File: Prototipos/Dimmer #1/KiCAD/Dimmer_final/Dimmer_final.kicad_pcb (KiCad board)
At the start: 2 copper layers, 50 x 100 mm, 1 part

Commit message: Avances PCB dimmer
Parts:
- removed the REF** at (95.5, 78.5)
- added C1: 330nF, Capacitor_THT:C_Disc_D10.5mm_W5.0mm_P7.50mm, F.Cu at (103.2, 56.5)
- added C2: 10nF, Capacitor_THT:C_Disc_D10.5mm_W5.0mm_P7.50mm, F.Cu at (130.8, 71.0)
- added D1: DB3, Diode_THT:D_DO-35_SOD27_P7.62mm_Horizontal, F.Cu at (103.5, 66.5)
- added D2: D_Small, Diode_THT:D_DO-41_SOD81_P7.62mm_Horizontal, F.Cu at (117.8, 127.1)
- added D3: D_Small, Diode_THT:D_DO-41_SOD81_P7.62mm_Horizontal, F.Cu at (123.5, 75.2)
- added J2: Conn_01x02, TerminalBlock_Phoenix:TerminalBlock_Phoenix_MKDS-1,5-2-5.08_1x02_P5.08mm_Horizontal, F.Cu at (137.5, 107.6)
- added J4: ~, Proyecto_Final:BUS_PCIE_x4_NSH, F.Cu at (95.5, 78.5)
- added K1: SRD-05VDC-SL-C, Relay_THT:Relay_SPDT_SANYOU_SRD_Series_Form_C, F.Cu at (113.5, 73.5)
- added Q1: BC548B, Package_TO_SOT_THT:TO-92_Inline_Wide, F.Cu at (123.5, 85.5)
- added Q2: BT137, Package_TO_SOT_THT:TO-220-3_Horizontal_TabDown, F.Cu at (137.1, 75.0)
- added R1: 47k, Resistor_THT:R_Axial_DIN0207_L6.3mm_D2.5mm_P7.62mm_Horizontal, F.Cu at (103.7, 60.5)
- added R10: 10k, Resistor_THT:R_Axial_DIN0207_L6.3mm_D2.5mm_P7.62mm_Horizontal, F.Cu at (107.2, 134.0)
- added R11: 33k, Resistor_THT:R_Axial_DIN0207_L6.3mm_D2.5mm_P7.62mm_Horizontal, F.Cu at (107.2, 137.5)
- added R2: 12k, Resistor_THT:R_Axial_DIN0207_L6.3mm_D2.5mm_P7.62mm_Horizontal, F.Cu at (116.0, 94.0)
- added R3: 100k, Potentiometer_THT:Potentiometer_Alps_RK09K_Single_Vertical, F.Cu at (117.5, 67.0)
- added R4: 470, Resistor_THT:R_Axial_DIN0207_L6.3mm_D2.5mm_P7.62mm_Horizontal, F.Cu at (111.3, 63.5)
- added R5: 82, Resistor_THT:R_Axial_DIN0207_L6.3mm_D2.5mm_P7.62mm_Horizontal, F.Cu at (107.2, 109.2)
- added R6: 10k, Resistor_THT:R_Axial_DIN0207_L6.3mm_D2.5mm_P7.62mm_Horizontal, F.Cu at (107.2, 118.5)
- added R7: 82, Resistor_THT:R_Axial_DIN0207_L6.3mm_D2.5mm_P7.62mm_Horizontal, F.Cu at (107.2, 112.2)
- added R8: 10k, Resistor_THT:R_Axial_DIN0207_L6.3mm_D2.5mm_P7.62mm_Horizontal, F.Cu at (107.2, 128.0)
- added R9: 51, Resistor_THT:R_Axial_DIN0207_L6.3mm_D2.5mm_P7.62mm_Horizontal, F.Cu at (138.5, 66.5)
- added REF**: MountingHole_2mm, MountingHole:MountingHole_2mm, F.Cu at (96.0, 49.0)
- added REF**: MountingHole_2mm, MountingHole:MountingHole_2mm, F.Cu at (96.0, 141.0)
- added REF**: MountingHole_2mm, MountingHole:MountingHole_2mm, F.Cu at (138.0, 49.0)
- added REF**: MountingHole_2mm, MountingHole:MountingHole_2mm, F.Cu at (138.0, 141.0)
- added U1: MOC3021M, ProyectoFinal:DIP762W45P254L889H508Q6, F.Cu at (110.8, 103.0)
- added U2: EL817, Package_DIP:DIP-4_W7.62mm, F.Cu at (114.9, 124.5)
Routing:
- net AGND: track 0.00 -> 148.9 mm
- net 48Vca_L: track 0.00 -> 129.4 mm
- net 48Vca_N: track 0.00 -> 86.8 mm
- net LOAD_L: track 0.00 -> 71.2 mm
- net 3.3Vcc: track 0.00 -> 49.9 mm
- net Net-(D1-A): track 0.00 -> 45.0 mm
- net IDENT_V: track 0.00 -> 44.9 mm
- net RELAY_T2: track 0.00 -> 32.9 mm
- net 5Vcc: track 0.00 -> 31.5 mm, vias 0 -> 2
- net Net-(J4-HP_Power): track 0.00 -> 23.6 mm
- net UC_RELAY: track 0.00 -> 20.7 mm, vias 0 -> 2
- net Net-(Q2-G): track 0.00 -> 20.3 mm
- net Net-(K1-Pad3): track 0.00 -> 14.2 mm
- net unconnected-(J4-12Vdc-Pad4): track 0.00 -> 13.7 mm
- net Net-(R1-Pad2): track 0.00 -> 13.1 mm
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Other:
- board text added: "Control analógico"
- board text added: "Control digital"
- board text added: "Ident. módulo"
- board text added: "Relé con driver"
- board text added: "TRIAC y Snubber"
- board text added: "ZCD"

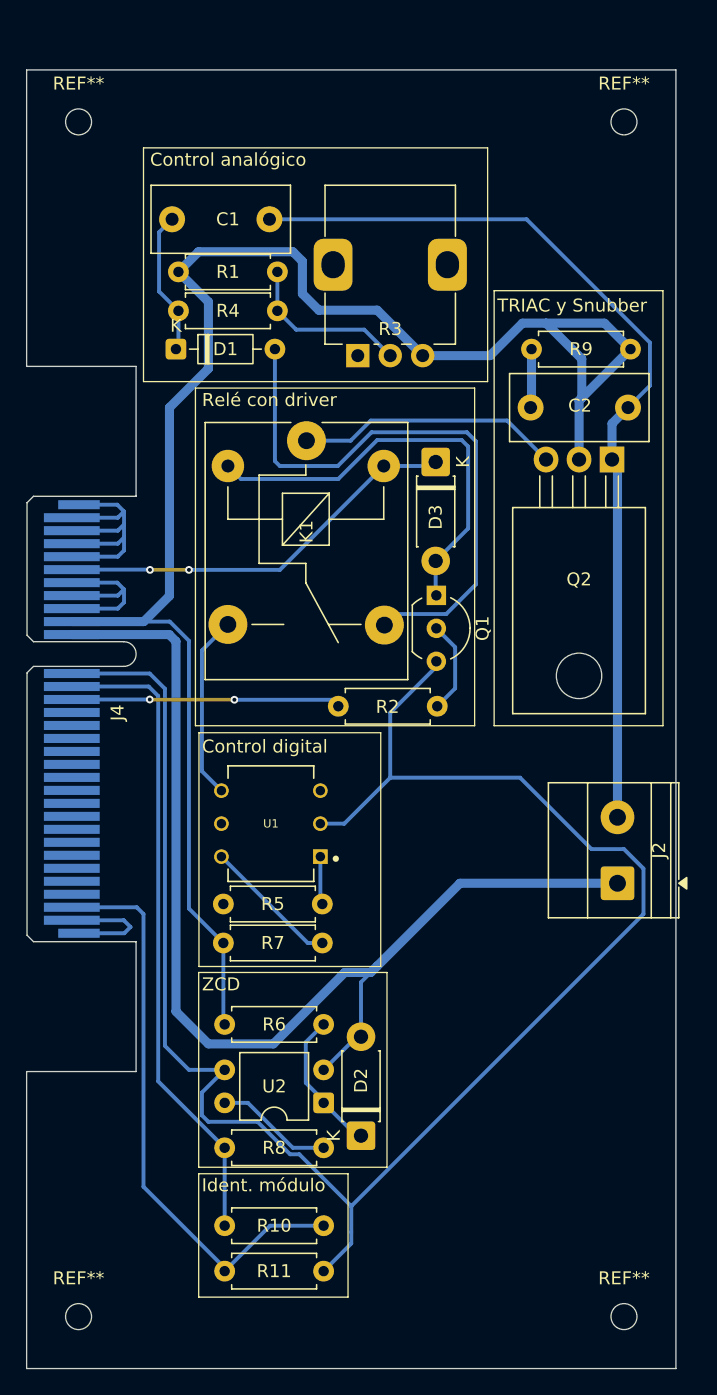
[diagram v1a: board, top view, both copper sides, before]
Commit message: Finalizar enrutamiento y primera versión inicial PCB
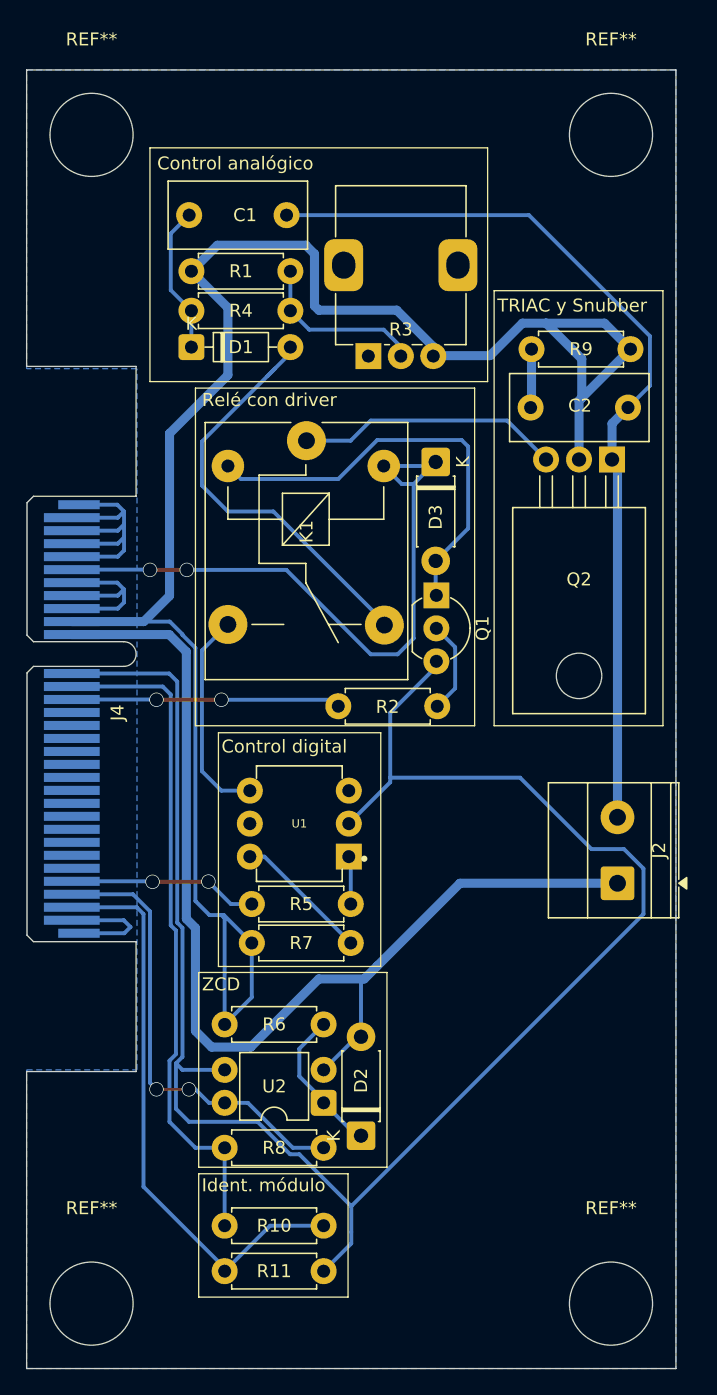
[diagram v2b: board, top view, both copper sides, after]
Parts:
- removed the REF** at (138.0, 141.0)
- added REF**: MountingHole_6.4mm_M6, MountingHole:MountingHole_6.4mm_M6, F.Cu at (137.0, 140.0)
- REF** (x3): value MountingHole_2mm -> MountingHole_6.4mm_M6; footprint MountingHole:MountingHole_2mm -> MountingHole:MountingHole_6.4mm_M6
- moved R5 2.19 mm to (109.3, 109.2)
- moved R7 2.19 mm to (109.3, 112.2)
- moved U1 2.19 mm to (113.0, 103.0)
- moved REF** 1.41 mm to (97.0, 50.0)
- moved REF** 1.41 mm to (97.0, 140.0)
- moved REF** 1.41 mm to (137.0, 50.0)
- moved C1 1.35 mm to (104.5, 56.2)
- moved D1 1.20 mm to (104.7, 66.3)
- moved R1 1.00 mm to (104.7, 60.5)
- moved R4 1.00 mm to (112.3, 63.5)
- moved R3 0.82 mm to (118.3, 67.0)
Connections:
- J4 pad 10: UC_PHASE -> unconnected-(J4-S2-Pad10)
- J4 pad 11: UC_DOUT -> unconnected-(J4-S3-Pad11)
- J4 pad 23: unconnected-(J4-S15-Pad23) -> UC_DOUT
- J4 pad 24: unconnected-(J4-S16-Pad24) -> UC_PHASE
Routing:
- net UC_PHASE: track 9.05 -> 35.2 mm, vias 0 -> 2
- net 5Vcc: track 31.5 -> 50.8 mm
- net UC_DOUT: track 0.00 -> 14.6 mm, vias 0 -> 2
- net 48Vca_L: track 129.4 -> 141.9 mm
- net Net-(D1-A): track 45.0 -> 32.9 mm
- net 3.3Vcc: track 49.9 -> 52.2 mm
- net Net-(K1-Pad3): track 14.2 -> 16.4 mm
- net AGND: track 148.9 -> 150.0 mm
- net LOAD_L: track 71.2 -> 70.3 mm
- added copper zone on B.Cu, net AGND

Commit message: Retoques finales placa dimmer
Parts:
- added TP1: TestPoint, TestPoint:TestPoint_Loop_D1.80mm_Drill1.0mm_Beaded, F.Cu at (132.0, 59.3)
- added TP2: TestPoint, TestPoint:TestPoint_Loop_D1.80mm_Drill1.0mm_Beaded, F.Cu at (126.9, 100.7)
- moved R7 0.15 mm to (109.3, 112.4)
- moved R5 0.08 mm to (109.3, 109.3)
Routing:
- net Net-(J4-HP_Power): track 23.6 -> 0.00 mm
- net unconnected-(J4-12Vdc-Pad4): track 13.7 -> 0.00 mm
- net LOAD_L: track 70.3 -> 83.3 mm
- net AGND: track 150.0 -> 141.1 mm
- net UC_PHASE: track 35.2 -> 43.5 mm
- net 48Vca_L: track 141.9 -> 140.8 mm
- added copper zone on B.Cu, net 5Vcc
- added copper zone on B.Cu, net Net-(J4-HP_Power)
- added copper zone on B.Cu, net unconnected-(J4-12Vdc-Pad4)

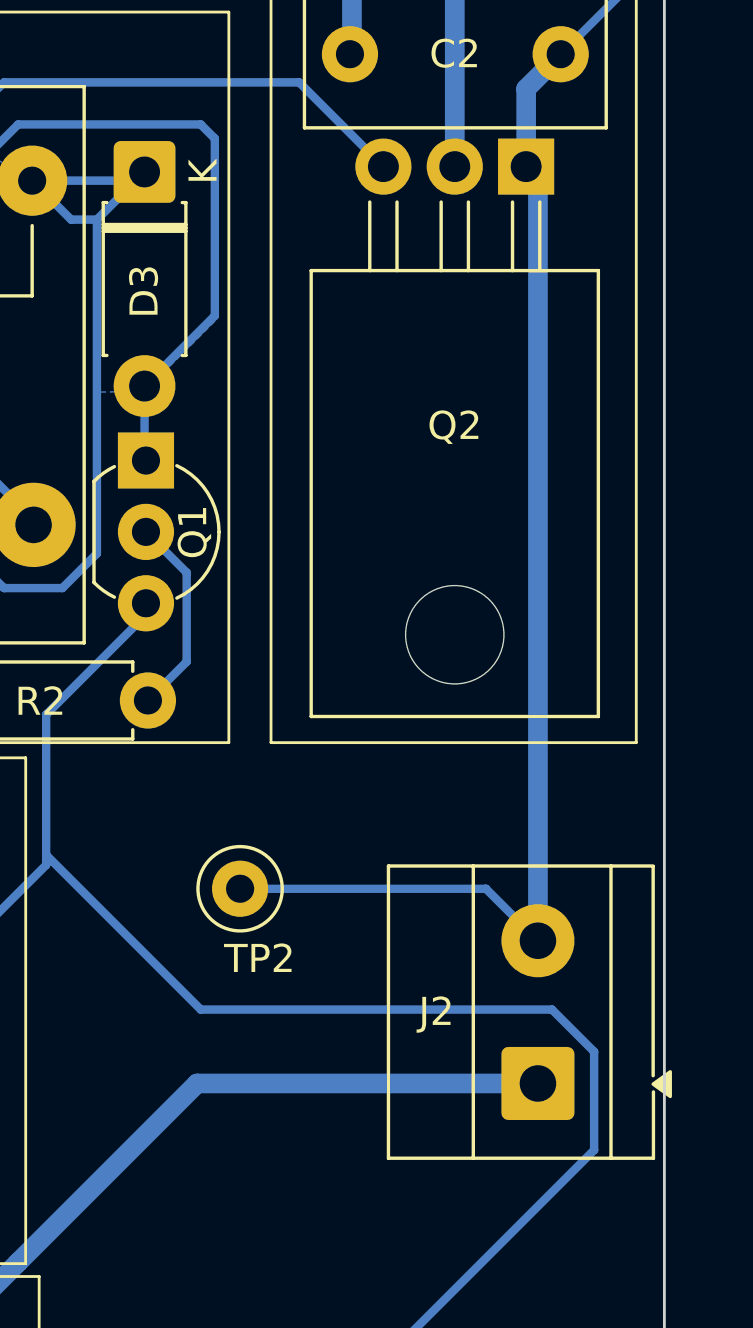
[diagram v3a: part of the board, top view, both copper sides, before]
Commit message: Mover bornera y modificar silkscreen footprint
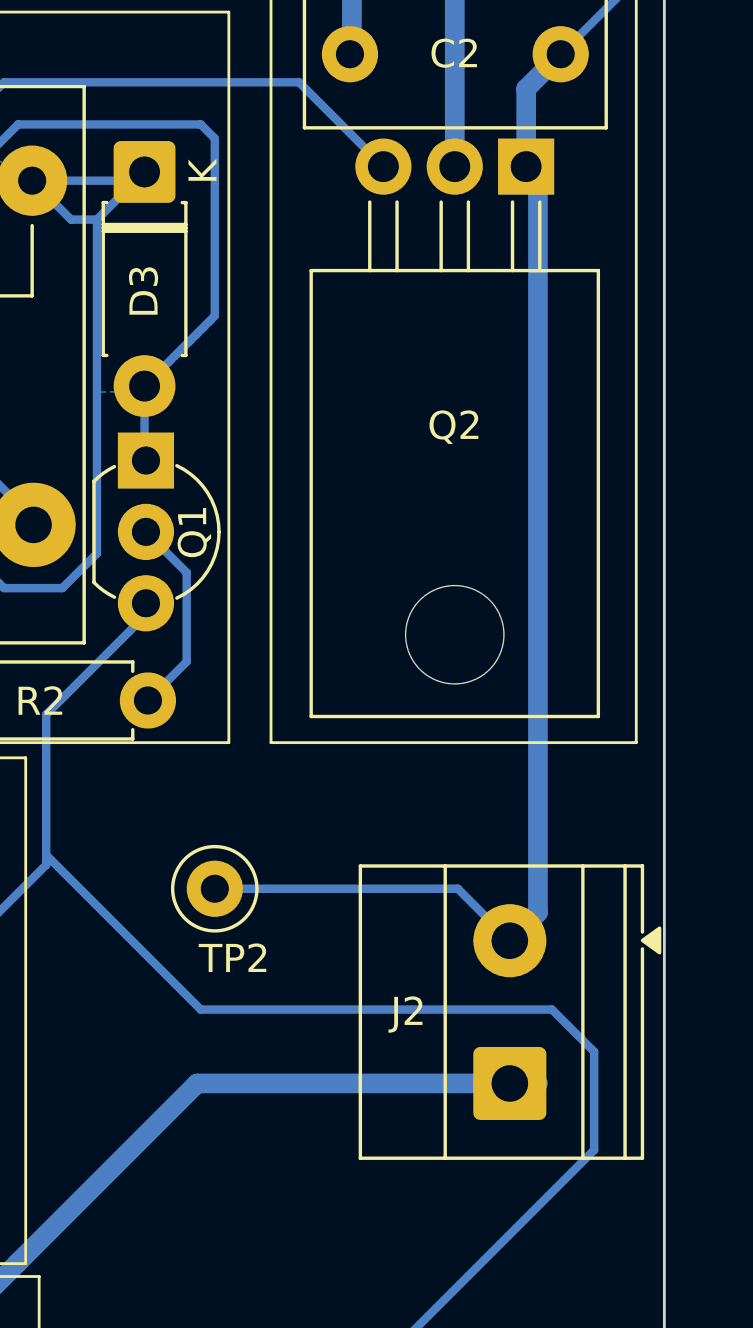
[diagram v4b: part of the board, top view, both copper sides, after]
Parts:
- moved J2 1.00 mm to (136.5, 107.6)
- moved TP2 0.90 mm to (126.0, 100.7)
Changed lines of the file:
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@@
 	(footprint "TestPoint:TestPoint_Loop_D1.80mm_Drill1.0mm_Beaded"
 		(layer "F.Cu")
-		(at 126.9 100.7)
+		(at 126 100.7)
 		(descr "wire loop with bead as test point, loop diameter 1.8mm, hole diameter 1.0mm")
 		(tags "test point wire loop bead")
@@
 	(footprint "TerminalBlock_Phoenix:TerminalBlock_Phoenix_MKDS-1,5-2-5.08_1x02_P5.08mm_Horizontal"
 		(layer "F.Cu")
-		(at 137.5 107.63 90)
+		(at 136.5 107.63 90)
 		(descr "Terminal Block Phoenix MKDS-1,5-2-5.08, 2 pins, pitch 5.08mm, size 10.2x9.8mm, drill diameter 1.3mm, pad diameter 2.6mm, http://www.farnell.com/datasheets/100425.pdf, script-generated using https://gitlab.com/kicad/libraries/kicad-footprint-generator/-/tree/master/scripts/TerminalBlock_Phoenix")
 		(tags "THT Terminal Block Phoenix MKDS-1,5-2-5.08 pitch 5.08mm size 10.2x9.8mm drill 1.3mm pad 2.6mm")
 		(property "Reference" "J2"
-			(at 2.544998 -3.610414 180)
+			(at 2.544998 -3.610414 0)
 			(layer "F.SilkS")
 			(effects
@@
 		(fp_line
 			(start 7.74 -5.32)
-			(end 7.74 4.1)
+			(end 7.74 4.72)
 			(stroke
 				(width 0.12)
@@
 		(fp_line
 			(start -2.66 -5.32)
-			(end -2.66 4.110795)
+			(end -2.66 4.72)
 			(stroke
 				(width 0.12)
@@
 		)
 		(fp_line
-			(start 0.276987 4.1)
-			(end 7.716987 4.1)
+			(start -2.66 4.1)
+			(end 7.74 4.1)
+			(stroke
+				(width 0.12)
+				(type solid)
+			)
+			(layer "F.SilkS")
+		)
+		(fp_line
+			(start 7.75 4.72)
+			(end 5.39 4.72)
 			(stroke
 				(width 0.12)
@@
 		)
 		(fp_line
-			(start -2.66 4.110795)
-			(end -0.3 4.110795)
+			(start 4.79 4.72)
+			(end -2.65 4.72)
 			(stroke
 				(width 0.12)
@@
 		(fp_poly
 			(pts
-				(xy -0.023013 4.1) (xy 0.416987 4.71) (xy -0.463013 4.71)
+				(xy 5.09 4.72) (xy 4.65 5.33) (xy 5.53 5.33)
 			)
 			(stroke
@@
 		)
 		(fp_text user "${REFERENCE}"
-			(at 2.54 -3.61 180)
+			(at 2.54 -3.61 0)
 			(layer "F.Fab")
 			(effects
@@
 	)
 	(segment
+		(start 137.5 101.55)
+		(end 137.5 75.42)
+		(width 0.7)
+		(layer "B.Cu")
+		(net 2)
+	)
+	(segment
 		(start 140.4 68.91)
 		(end 138.31 71)
@@
 	)
 	(segment
+		(start 136.5 102.55)
+		(end 134.65 100.7)
+		(width 0.3)
+		(layer "B.Cu")
+		(net 2)
+	)
+	(segment
 		(start 140.4 63.7)
 		(end 140.4 68.91)
@@
 	)
 	(segment
-		(start 137.5 102.55)
-		(end 137.5 75.42)
+		(start 137.08 75)
+		(end 137.08 72.23)
 		(width 0.7)
 		(layer "B.Cu")
@@
 	)
 	(segment
-		(start 135.65 100.7)
-		(end 137.5 102.55)
-		(width 0.3)
-		(layer "B.Cu")
-		(net 2)
-	)
-	(segment
-		(start 137.08 75)
-		(end 137.08 72.23)
+		(start 137.08 72.23)
+		(end 138.31 71)
 		(width 0.7)
 		(layer "B.Cu")
@@
 	)
 	(segment
-		(start 137.08 72.23)
-		(end 138.31 71)
+		(start 136.5 102.55)
+		(end 137.5 101.55)
 		(width 0.7)
 		(layer "B.Cu")
@@
 	)
 	(segment
-		(start 126.9 100.7)
-		(end 135.65 100.7)
+		(start 112.016536 56.181903)
+		(end 132.881903 56.181903)
 		(width 0.3)
 		(layer "B.Cu")
@@
 	)
 	(segment
-		(start 112.016536 56.181903)
-		(end 132.881903 56.181903)
+		(start 134.65 100.7)
+		(end 126 100.7)
 		(width 0.3)
 		(layer "B.Cu")

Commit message: Agregar M4s a la derecha y retoques generales
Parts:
- M4_H, M4_L: renamed from REF**; value MountingHole_6.4mm_M6 -> MountingHole_4.3mm_M4; footprint MountingHole:MountingHole_6.4mm_M6 -> MountingHole:MountingHole_4.3mm_M4
- moved M4_H 1.41 mm to (138.0, 49.0)
- moved M4_L 1.41 mm to (138.0, 141.0)
- moved M6_H 1.41 mm to (96.0, 49.0)
- moved M6_L 1.41 mm to (96.0, 141.0)
- renumbered REF** to M6_H, REF** to M6_L
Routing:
- net 48Vca_L: track 140.8 -> 134.5 mm
- net 5Vcc: track 50.8 -> 48.0 mm
- net 48Vca_N: track 87.0 -> 86.4 mm
- added copper zone on B.Cu, net 48Vca_N

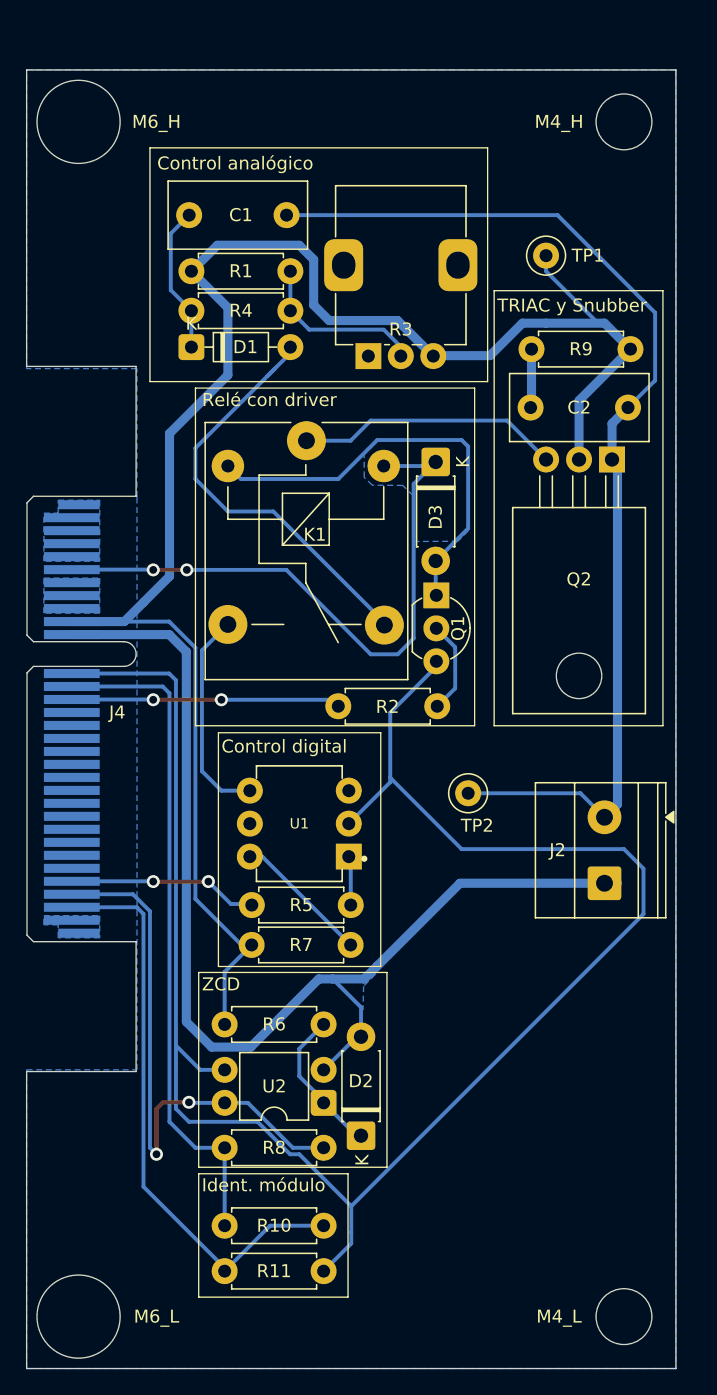
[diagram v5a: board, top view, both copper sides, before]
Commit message: Agregar TPs nuevos y correcciones varias
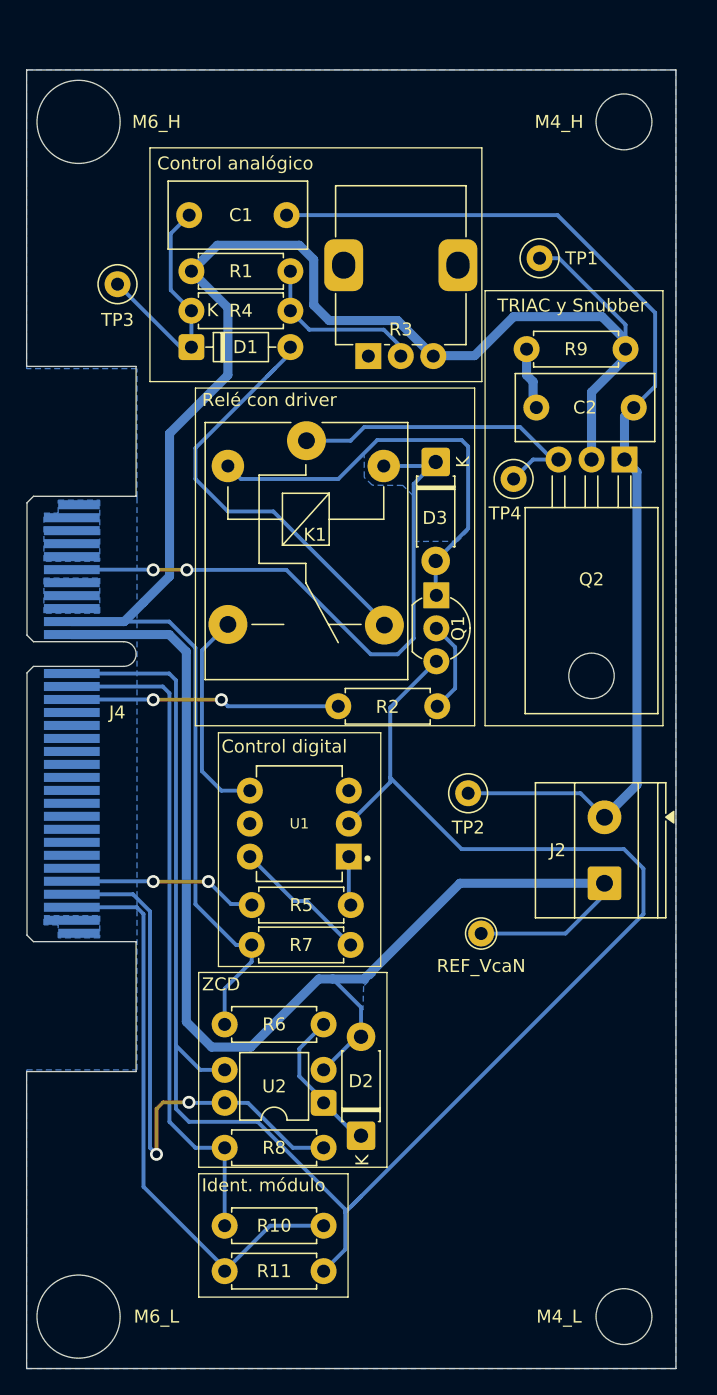
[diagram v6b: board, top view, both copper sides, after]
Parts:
- added REF_VcaN: TestPoint_THTPad_D2.0mm_Drill1.0mm, TestPoint:TestPoint_THTPad_D2.0mm_Drill1.0mm, F.Cu at (127.0, 111.5)
- added TP3: TestPoint, TestPoint:TestPoint_Loop_D1.80mm_Drill1.0mm_Beaded, F.Cu at (99.0, 61.5)
- added TP4: TestPoint, TestPoint:TestPoint_Loop_D1.80mm_Drill1.0mm_Beaded, F.Cu at (129.5, 76.5)
- moved Q2 0.96 mm to (138.0, 75.0)
- moved TP1 0.54 mm to (131.5, 59.5)
- moved C2 0.44 mm to (131.2, 71.0)
- moved R9 0.38 mm to (138.1, 66.5)
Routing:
- net 48Vca_N: track 86.4 -> 97.1 mm
- net Net-(D1-K): track 11.4 -> 19.1 mm
- net Net-(Q2-G): track 20.3 -> 25.0 mm
- net 48Vca_L: track 134.5 -> 137.9 mm
- net AGND: track 141.3 -> 142.2 mm
- net LOAD_L: track 83.6 -> 84.5 mm
